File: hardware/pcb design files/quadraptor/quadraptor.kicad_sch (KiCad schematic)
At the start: 146 parts, among them J1 Conn_01x04, J10 Conn_01x04, J11 Conn_02x09_Odd_Even, J12 Conn_02x04, J13 Conn_01x04, J14 Conn_01x02, J15 Conn_01x02, J16 Conn_01x02, J17 Conn_01x02, J18 Conn_01x02, J19 Conn_01x04, J2 Conn_01x02, J20 Conn_01x04, J21 Conn_01x04, J22 Conn_01x04, J23 Conn_01x06, J24 Conn_01x04, J25 Conn_01x02, J3 USB_C_Receptacle_USB2.0, J4 Micro_SD_Card, J5 Conn_01x06, J6 Conn_01x03, J7 Conn_01x03, J8 Conn_01x03, J9 Conn_01x03, Q1 TIP121, SW1 SW_Push, SW2 SW_Push, SW3 SW_DIP_x01, SW4 SW_SPDT, U1 CH32V203C8T6, U10 MPU-6050, U11 AMS1117-5.0, U12 AMS1117-3.3, U14 MCP4921-EMC, U2 CH32V203C8T6, U3 ADXL345BCCZ, U4 BMP280, U6 HMC5883L, U7 AMS1117-3.3, U8 PAM8403D, U9 AMS1117-5.0, Y1 8 MHZ, Y2 8 MHZ

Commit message: [UPDATE]: reverted back pcb file of kicad
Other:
- note added: "ADC1[4]"
- note added: "CH1"
- note added: "CH2"
- note added: "CH3"
- note added: "CH4"
- note added: "I2C2"
- note added: "TIM4"
- moved on the sheet: J24
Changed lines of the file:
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@@
     (stroke (width 0) (type default))
   )
-  (wire (pts (xy 582.93 132.08) (xy 601.98 132.08))
+  (wire (pts (xy 577.85 132.08) (xy 601.98 132.08))
     (stroke (width 0) (type default))
   )
@@
     (stroke (width 0) (type default))
   )
-  (wire (pts (xy 627.38 161.29) (xy 627.38 162.56))
+  (wire (pts (xy 615.95 162.56) (xy 615.95 163.83))
     (stroke (width 0) (type default))
   )
@@
     (stroke (width 0) (type default))
   )
-  (wire (pts (xy 624.84 144.78) (xy 638.81 144.78))
+  (wire (pts (xy 619.76 144.78) (xy 638.81 144.78))
     (stroke (width 0) (type default))
   )
@@
     (stroke (width 0) (type default))
   )
-  (wire (pts (xy 627.38 162.56) (xy 635 162.56))
+  (wire (pts (xy 615.95 163.83) (xy 623.57 163.83))
     (stroke (width 0) (type default))
   )
@@
     (stroke (width 0) (type default))
   )
-  (wire (pts (xy 626.11 161.29) (xy 627.38 161.29))
+  (wire (pts (xy 614.68 162.56) (xy 615.95 162.56))
     (stroke (width 0) (type default))
   )
@@
     (stroke (width 0) (type default))
   )
-  (wire (pts (xy 624.84 132.08) (xy 638.81 132.08))
+  (wire (pts (xy 619.76 132.08) (xy 638.81 132.08))
     (stroke (width 0) (type default))
   )
@@
     (stroke (width 0) (type default))
   )
-  (wire (pts (xy 612.14 167.64) (xy 635 167.64))
+  (wire (pts (xy 600.71 168.91) (xy 623.57 168.91))
     (stroke (width 0) (type default))
   )
@@
     (stroke (width 0) (type default))
   )
-  (wire (pts (xy 582.93 144.78) (xy 601.98 144.78))
+  (wire (pts (xy 577.85 144.78) (xy 601.98 144.78))
     (stroke (width 0) (type default))
   )
@@
     (stroke (width 0) (type default))
   )
-  (wire (pts (xy 627.38 170.18) (xy 635 170.18))
+  (wire (pts (xy 615.95 171.45) (xy 623.57 171.45))
     (stroke (width 0) (type default))
   )
@@
     (stroke (width 0) (type default))
   )
-  (wire (pts (xy 612.14 165.1) (xy 635 165.1))
+  (wire (pts (xy 600.71 166.37) (xy 623.57 166.37))
     (stroke (width 0) (type default))
   )
@@
     (fill (type none))
   )
-  (text "UART interface with \napplication board" (at 603.25 80.01 0)
+  (text "UART interface with \napplication board" (at 598.17 80.01 0)
     (effects (font (size 1.27 1.27)) (justify left bottom))
   )
@@
     (effects (font (size 1.27 1.27)) (justify left bottom))
   )
+  (text "CH3" (at 633.73 132.08 0)
+    (effects (font (size 1.27 1.27)) (justify left bottom))
+  )
   (text "battery monitor" (at 392.43 57.15 0)
     (effects (font (size 3 3)) (justify left bottom))
@@
     (effects (font (size 1.27 1.27)) (justify left bottom))
   )
-  (text "RX" (at 633.73 165.1 0)
+  (text "RX" (at 622.3 166.37 0)
     (effects (font (size 1.27 1.27)) (justify left bottom))
   )
@@
     (effects (font (size 1.27 1.27)) (justify left bottom))
   )
-  (text "TX" (at 633.73 167.64 0)
+  (text "TX" (at 622.3 168.91 0)
     (effects (font (size 1.27 1.27)) (justify left bottom))
   )
@@
     (effects (font (size 3 3)) (justify left bottom))
   )
+  (text "CH2" (at 596.9 144.78 0)
+    (effects (font (size 1.27 1.27)) (justify left bottom))
+  )
   (text "CNS" (at 576.58 453.39 0)
     (effects (font (size 1.27 1.27)) (justify left bottom))
   )
-  (text "Ultrasound sensors" (at 610.87 186.69 0)
+  (text "Ultrasound sensors" (at 605.79 186.69 0)
     (effects (font (size 1.27 1.27)) (justify left bottom))
   )
@@
     (effects (font (size 1.27 1.27)) (justify left bottom))
   )
-  (text "GPS interface" (at 610.87 158.75 0)
+  (text "GPS interface" (at 599.44 160.02 0)
     (effects (font (size 1.27 1.27)) (justify left bottom))
   )
@@
     (effects (font (size 3 3)) (justify left bottom))
   )
-  (text "MCU (CH32V203C8T6)" (at 45.72 307.34 0)
+  (text "ADC1[4]" (at 400.05 81.28 0)
+    (effects (font (size 2 2)) (justify left bottom))
+  )
+  (text "MCU (CH32V203C8T6)" (at 49.53 307.34 0)
     (effects (font (size 3 3)) (justify left bottom))
   )
@@
     (effects (font (size 3 3)) (justify left bottom))
   )
+  (text "I2C2" (at 293.37 78.74 0)
+    (effects (font (size 2 2)) (justify left bottom))
+  )
   (text "D1" (at 557.53 430.53 0)
     (effects (font (size 1.27 1.27)) (justify left bottom))
@@
     (effects (font (size 1.27 1.27)) (justify left bottom))
   )
+  (text "CH4" (at 633.73 144.78 0)
+    (effects (font (size 1.27 1.27)) (justify left bottom))
+  )
   (text "fast mode of I2C is used" (at 318.77 93.98 0)
     (effects (font (face "KiCad Font") (size 1.27 1.27)) (justify left bottom))
@@
     (effects (font (size 3 3)) (justify left bottom))
   )
+  (text "CH1" (at 596.9 132.08 0)
+    (effects (font (size 1.27 1.27)) (justify left bottom))
+  )
   (text "MOSI" (at 294.64 382.27 0)
     (effects (font (size 1.27 1.27)) (justify left bottom))
@@
     (effects (font (size 1.27 1.27)) (justify left bottom))
   )
+  (text "TIM4" (at 577.85 128.27 0)
+    (effects (font (size 2 2)) (justify left bottom))
+  )
   (text "LED control" (at 389.89 307.34 0)
     (effects (font (size 3 3)) (justify left bottom))
@@
     (effects (font (size 1.27 1.27)) (justify left bottom))
   )
-  (label "U1_PB7_USB2DP" (at 582.93 144.78 0) (fields_autoplaced)
+  (label "U1_PB7_USB2DP" (at 577.85 144.78 0) (fields_autoplaced)
     (effects (font (size 1.27 1.27)) (justify left bottom))
   )
@@
     (effects (font (size 1.27 1.27)) (justify right bottom))
   )
-  (label "U1_PB9" (at 624.84 144.78 0) (fields_autoplaced)
+  (label "U1_PB9" (at 619.76 144.78 0) (fields_autoplaced)
     (effects (font (size 1.27 1.27)) (justify left bottom))
   )
@@
     (effects (font (size 1.27 1.27)) (justify left bottom))
   )
-  (label "U1_PB6_USB2DM" (at 582.93 132.08 0) (fields_autoplaced)
+  (label "U1_PB6_USB2DM" (at 577.85 132.08 0) (fields_autoplaced)
     (effects (font (size 1.27 1.27)) (justify left bottom))
   )
@@
     (effects (font (size 1.27 1.27)) (justify right bottom))
   )
-  (label "U1_PA10" (at 612.14 167.64 0) (fields_autoplaced)
+  (label "U1_PA10" (at 600.71 168.91 0) (fields_autoplaced)
     (effects (font (size 1.27 1.27)) (justify left bottom))
   )
@@
     (effects (font (size 1.27 1.27)) (justify left bottom))
   )
-  (label "U1_PB8" (at 624.84 132.08 0) (fields_autoplaced)
+  (label "U1_PB8" (at 619.76 132.08 0) (fields_autoplaced)
     (effects (font (size 1.27 1.27)) (justify left bottom))
   )
@@
     (effects (font (size 1.27 1.27)) (justify left bottom))
   )
-  (label "U1_PA9" (at 612.14 165.1 0) (fields_autoplaced)
+  (label "U1_PA9" (at 600.71 166.37 0) (fields_autoplaced)
     (effects (font (size 1.27 1.27)) (justify left bottom))
   )
@@
     )
   )
-  (global_label "GND_Dboard" (shape input) (at 627.38 170.18 180) (fields_autoplaced)
+  (global_label "GND_Dboard" (shape input) (at 615.95 171.45 180) (fields_autoplaced)
     (effects (font (size 1.27 1.27)) (justify right))
-    (property "Intersheetrefs" "${INTERSHEET_REFS}" (at 612.9839 170.18 0)
+    (property "Intersheetrefs" "${INTERSHEET_REFS}" (at 601.5539 171.45 0)
       (effects (font (size 1.27 1.27)) (justify right) hide)
     )
@@
     )
   )
-  (global_label "3.3V_Dboard" (shape input) (at 626.11 161.29 180) (fields_autoplaced)
+  (global_label "3.3V_Dboard" (shape input) (at 614.68 162.56 180) (fields_autoplaced)
     (effects (font (size 1.27 1.27)) (justify right))
-    (property "Intersheetrefs" "${INTERSHEET_REFS}" (at 611.472 161.29 0)
+    (property "Intersheetrefs" "${INTERSHEET_REFS}" (at 600.042 162.56 0)
       (effects (font (size 1.27 1.27)) (justify right) hide)
     )
@@
     )
   )
-  (symbol (lib_id "Connector_Generic:Conn_01x04") (at 640.08 165.1 0) (unit 1)
+  (symbol (lib_id "Connector_Generic:Conn_01x04") (at 628.65 166.37 0) (unit 1)
     (in_bom yes) (on_board yes) (dnp no) (fields_autoplaced)
-    (property "Reference" "J24" (at 642.62 165.735 0)
+    (property "Reference" "J24" (at 631.19 167.005 0)
       (effects (font (size 1.27 1.27)) (justify left))
     )
-    (property "Value" "Conn_01x04" (at 642.62 168.275 0)
+    (property "Value" "Conn_01x04" (at 631.19 169.545 0)
       (effects (font (size 1.27 1.27)) (justify left))
     )
-    (property "Footprint" "Connector_JST:JST_XH_B4B-XH-A_1x04_P2.50mm_Vertical" (at 640.08 165.1 0)
+    (property "Footprint" "Connector_JST:JST_XH_B4B-XH-A_1x04_P2.50mm_Vertical" (at 628.65 166.37 0)
       (effects (font (size 1.27 1.27)) hide)
     )
-    (property "Datasheet" "~" (at 640.08 165.1 0)
+    (property "Datasheet" "~" (at 628.65 166.37 0)
       (effects (font (size 1.27 1.27)) hide)
     )
-    (property "Purpose" "" (at 640.08 165.1 0)
+    (property "Purpose" "" (at 628.65 166.37 0)
       (effects (font (size 1.27 1.27)))
     )

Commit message: [UPDATE]: create the skeleton project from the drone board
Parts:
- removed J3: USB_C_Receptacle_USB2.0, Connector_USB:USB_C_Receptacle_XKB_U262-16XN-4BVC11, symbol Connector:USB_C_Receptacle_USB2.0
- added J26: TYPE-C-31-M-12, TYPE-C-31-M-12:HRO_TYPE-C-31-M-12, symbol TYPE-C-31-M-12:TYPE-C-31-M-12
- D5, D6: footprint Diode_SMD:D_SOD-323 -> Diode_SMD:D_SMA
- U14: footprint Package_DFN_QFN:DFN-8-1EP_3x2mm_P0.5mm_EP1.75x1.45mm -> Package_SO:MSOP-8-1EP_3x3mm_P0.65mm_EP1.68x1.88mm
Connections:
- net GND_APPboard: now also J26.A1_B12 (GND), J26.B1_A12 (GND), J26.S1 (SHIELD), J26.S2 (SHIELD), J26.S3 (SHIELD), J26.S4 (SHIELD)
- net U1_PA11_USB1DM: now also J21.3 (Pin_3); no longer U6.15 (DRDY)
- net U1_PA1_ADC1: now also J20.3 (Pin_3); no longer U3.9 (INT2)
- net U1_PB12: now also U6.15 (DRDY); no longer J21.3 (Pin_3)
- net U1_PB14: now also U3.9 (INT2); no longer J20.3 (Pin_3)
- net U2_PB6_USB2DM: now also J26.A7 (DN1), J26.B7 (DN2)
- net U2_PB7_USB2DP: now also J26.A6 (DP1), J26.B6 (DP2)
- net usb_vbus: now also J26.A4_B9 (VBUS), J26.B4_A9 (VBUS)
- net at R7.1: now also J26.B5 (CC2)
- net at R6.1: now also J26.A5 (CC1)
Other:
- note added: "max speed (ADXL345) = 5Mbps"
- moved on the sheet: J13, J14, J25, J5, TP17

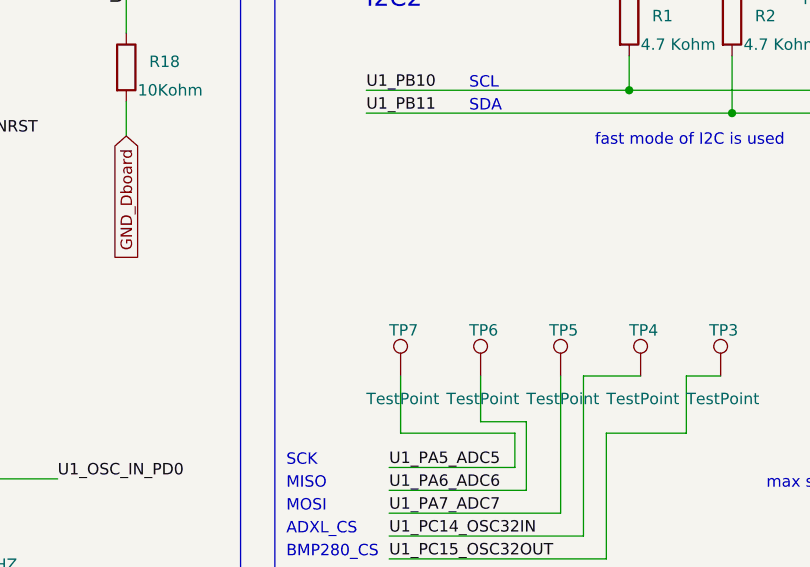
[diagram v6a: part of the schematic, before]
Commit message: [UPDATE]: changed clock value of PCLK1 to be 144 MHZ instead of 72 MHZ and added some configurations to the SPI of ADXL345
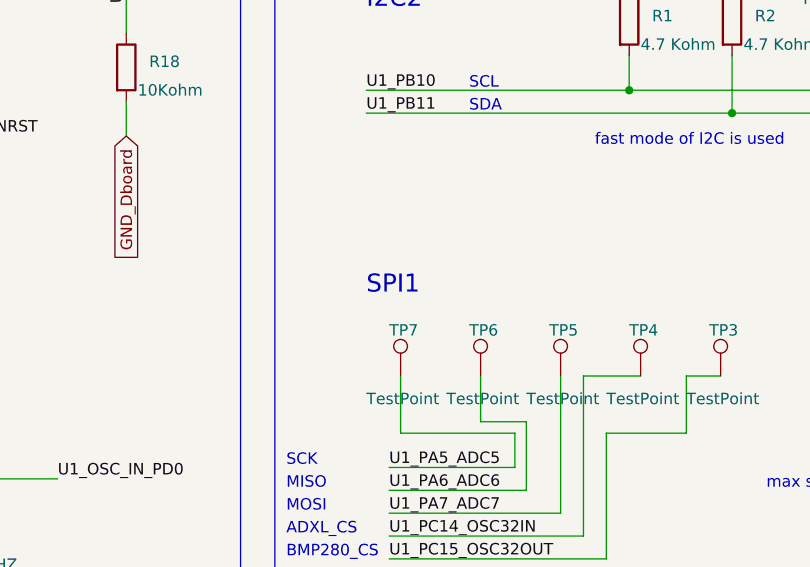
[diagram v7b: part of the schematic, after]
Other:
- note added: "SPI1"
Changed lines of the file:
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@@
     (effects (font (size 1.27 1.27)) (justify left bottom))
+  )
+  (text "SPI1" (at 293.37 110.49 0)
+    (effects (font (size 2 2)) (justify left bottom))
   )
   (text "ADXL_CS" (at 284.48 137.16 0)
